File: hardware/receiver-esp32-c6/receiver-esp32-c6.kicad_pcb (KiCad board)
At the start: 4 copper layers, 40 x 70 mm, 47 parts, among them J1 Conn_01x03, J10 Conn_01x04, J11 Conn_01x03, J2 Conn_01x03, J3 Conn_01x03, J4 Conn_01x06, J5 Conn_01x06, J6 Conn_01x02, J7 Conn_02x04_Counter_Clockwise, J8 Conn_02x03_Counter_Clockwise, J9 Conn_01x04, SW1 SW_Push_DPDT, SW2 SW_Push, U1 ESP32-C6-WROOM-1, U2 ULN2003, U3 MT3608, U4 MT3608, U5 INA226

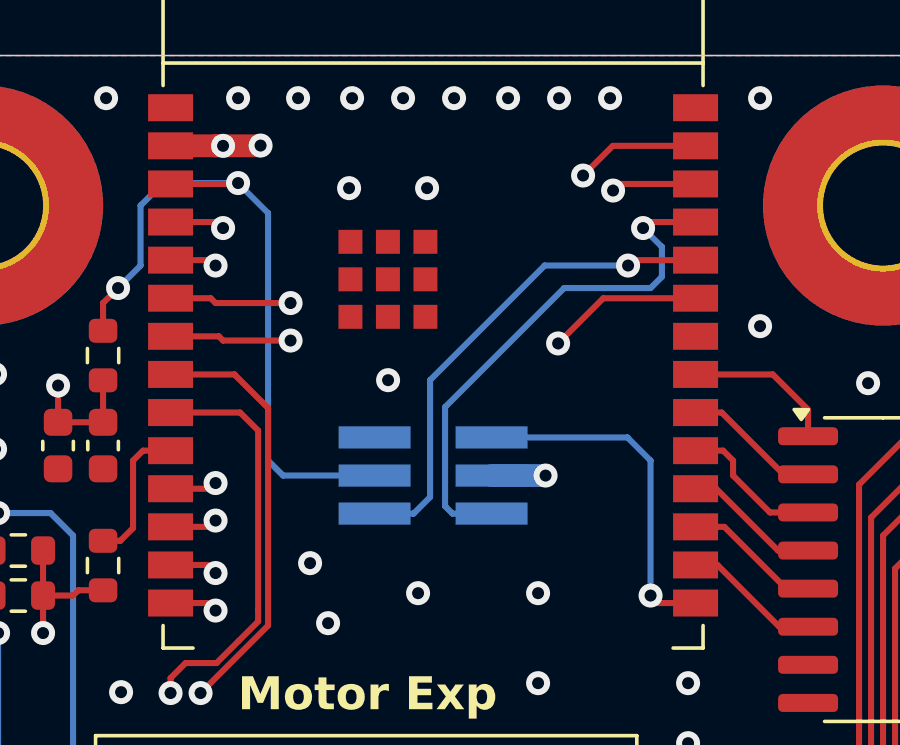
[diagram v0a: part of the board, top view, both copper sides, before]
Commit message: Fixed the ESP-PROG pinout
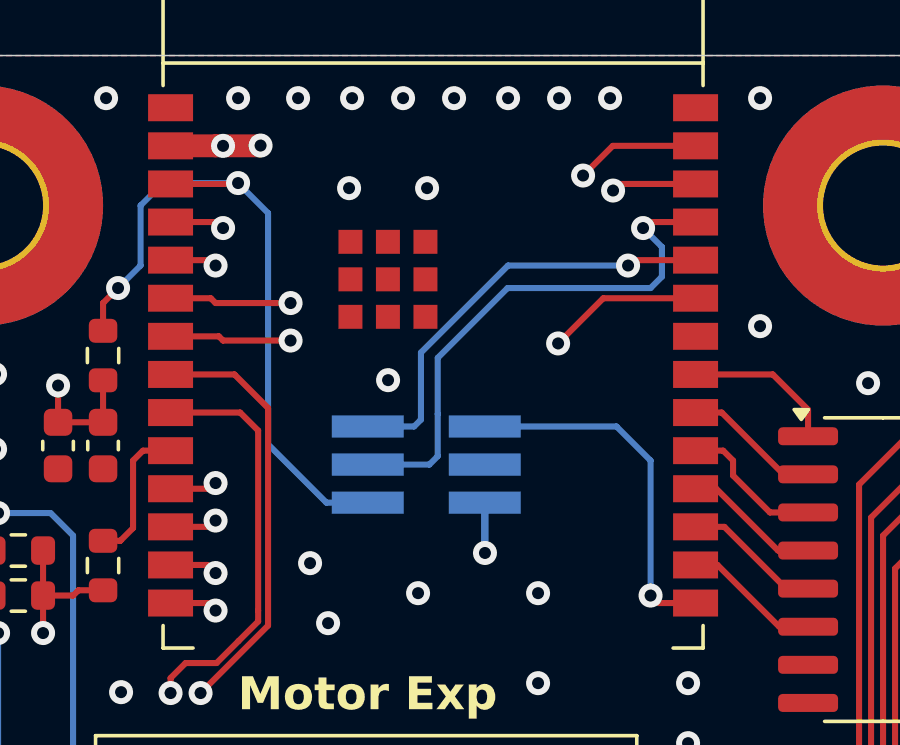
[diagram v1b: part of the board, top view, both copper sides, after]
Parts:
- removed J8: Conn_02x03_Counter_Clockwise, Connector_PinHeader_1.27mm:PinHeader_2x03_P1.27mm_Vertical_SMD
- added J12: Conn_02x03_Odd_Even, Connector_PinHeader_1.27mm:PinHeader_2x03_P1.27mm_Vertical_SMD, B.Cu at (142.3, 66.1)
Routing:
- net UART_RX: track 16.5 -> 14.5 mm
